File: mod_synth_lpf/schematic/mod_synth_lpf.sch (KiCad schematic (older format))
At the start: 47 parts

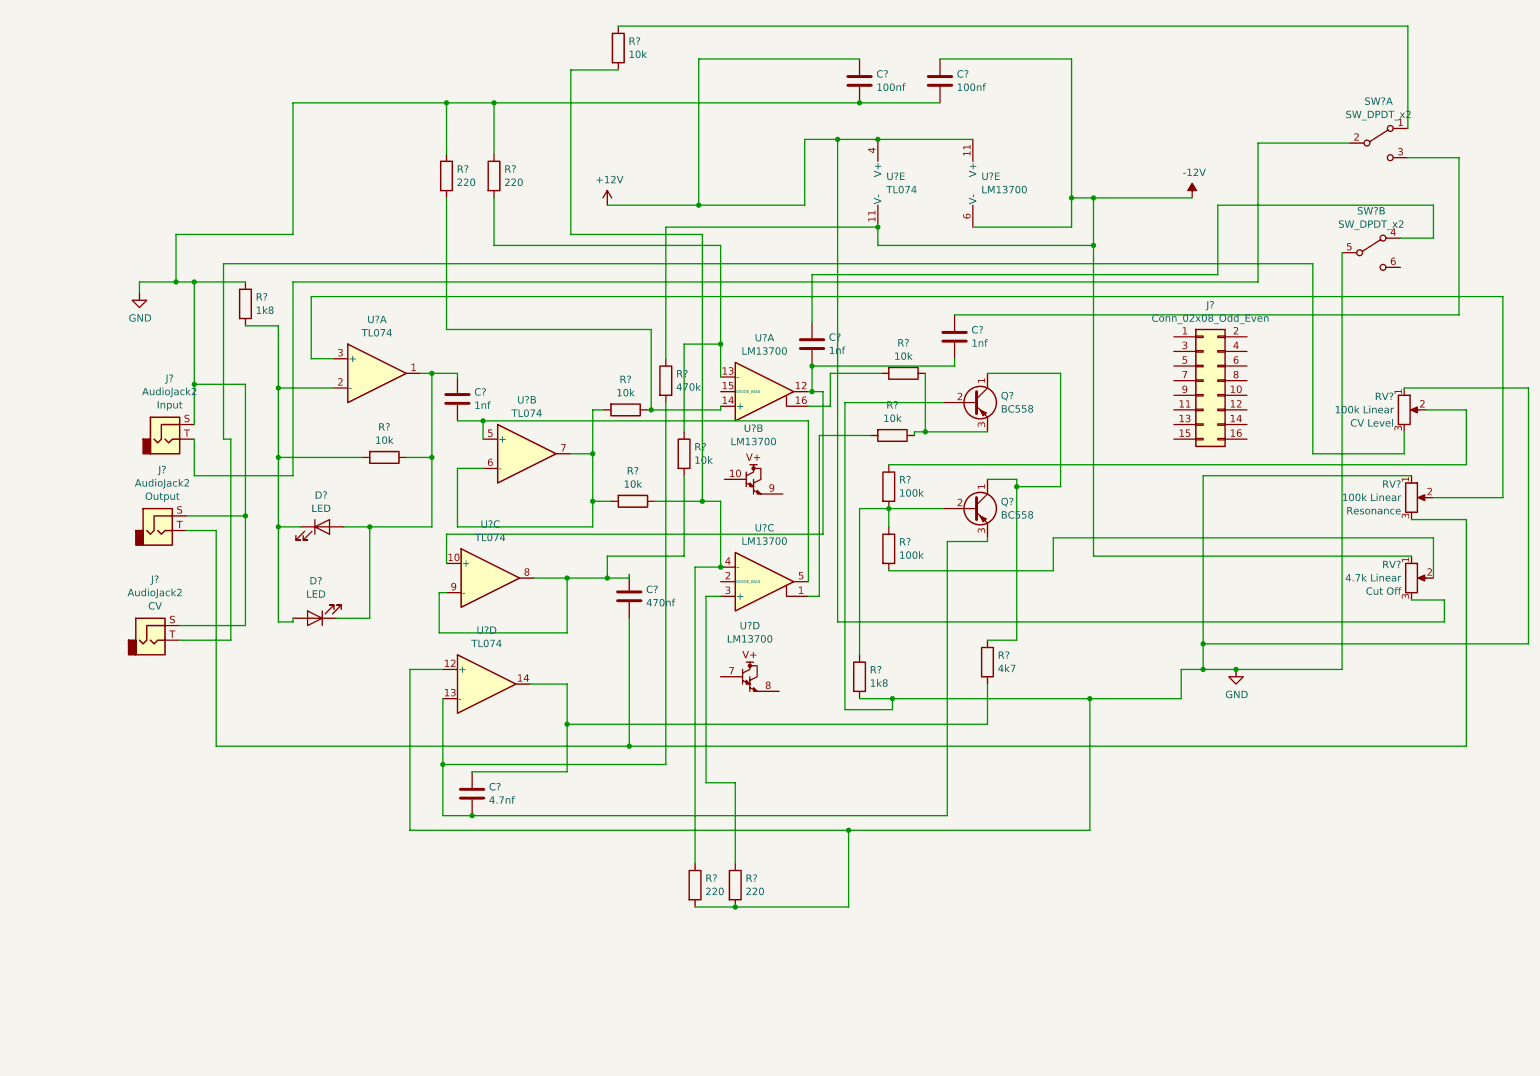
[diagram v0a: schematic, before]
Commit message: Add some footprints to LPF
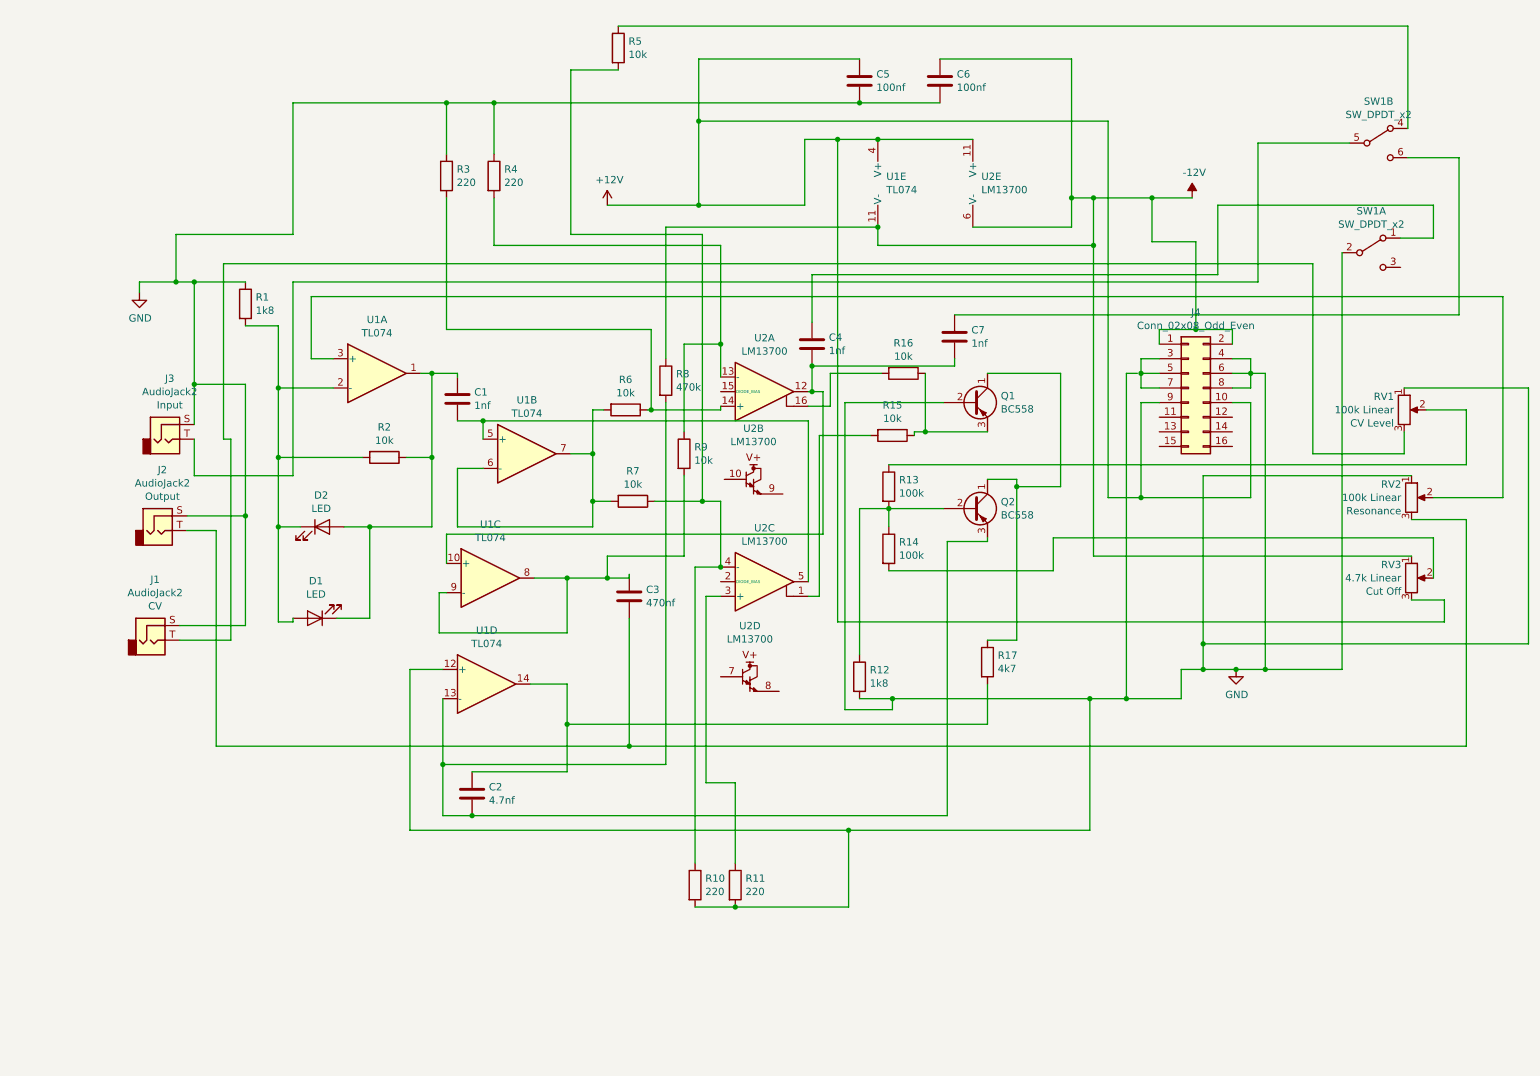
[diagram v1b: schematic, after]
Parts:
- J4: renamed from J?; footprint (none) -> Connector_IDC:IDC-Header_2x08_P2.54mm_Vertical
- RV1, RV2, RV3: renamed from RV?; footprint (none) -> Potentiometer_THT:Potentiometer_Alpha_RD901F-40-00D_Single_Vertical_CircularHoles
- gave numbers to parts that had none: 34
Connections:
- net +12V: now also J4.10 (Pin_10), J4.9 (Pin_9)
- net -12V: now also J4.1 (Pin_1), J4.2 (Pin_2)
- net GND: now also J4.4 (Pin_4), J4.6 (Pin_6), J4.8 (Pin_8), SW1.2 (B); no longer SW1.5 (B)
- net at J4.3 (Pin_3): now also J4.5 (Pin_5), J4.7 (Pin_7)
- net at J3.T: now also SW1.5 (B); no longer SW1.2 (B)
- net at C4.1: now also SW1.1 (A); no longer SW1.4 (A)
- net at C7.1: now also SW1.6 (C); no longer SW1.3 (C)
- net at R5.1: now also SW1.4 (A); no longer SW1.1 (A)
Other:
- moved on the sheet: J4

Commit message: Organise schematic and cram components on PCB
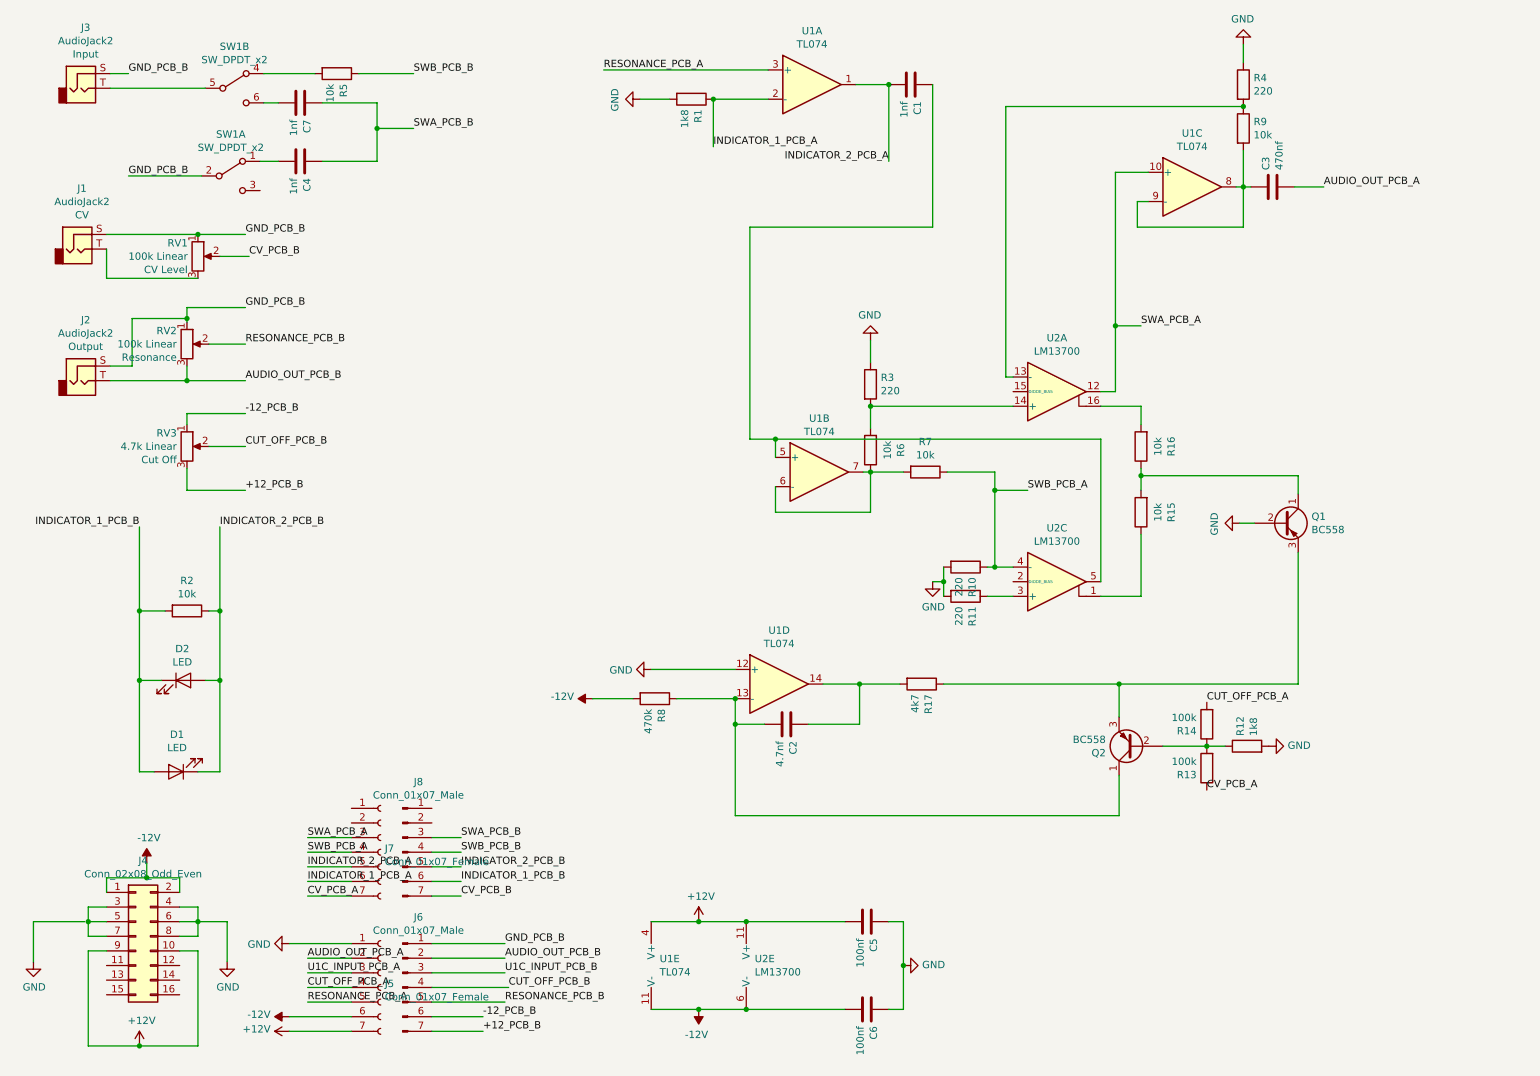
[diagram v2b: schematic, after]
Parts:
- removed unit 2 of U2
- removed unit 4 of U2
- added J5, J7: Conn_01x07_Female, Connector_PinSocket_2.54mm:PinSocket_1x07_P2.54mm_Vertical, symbol Connector:Conn_01x07_Female
- added J6, J8: Conn_01x07_Male, Connector_PinHeader_2.54mm:PinHeader_1x07_P2.54mm_Vertical, symbol Connector:Conn_01x07_Male
- C1, C2, C3, C4, C5, C6, C7: footprint (none) -> Capacitor_THT:C_Disc_D9.0mm_W2.5mm_P5.00mm
- D1, D2: footprint (none) -> LED_THT:LED_D5.0mm
- J1, J2, J3: footprint (none) -> Connector_Audio:Jack_3.5mm_QingPu_WQP-PJ398SM_Vertical_CircularHoles
- R1, R10, R11, R12, R13, R14, R15, R16, R17, R2, R3, R4, R5, R6, R7, R8, R9: footprint (none) -> Resistor_THT:R_Axial_DIN0207_L6.3mm_D2.5mm_P10.16mm_Horizontal
- SW1: footprint (none) -> mod_synth:DPDT_Switch_Vertical
- U1: footprint (none) -> Package_DIP:DIP-14_W7.62mm_Socket_LongPads
- U2: footprint (none) -> Package_DIP:DIP-18_W7.62mm_Socket_LongPads
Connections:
- net +12V: now also C5.2, J5.7 (Pin_7); no longer C5.1, RV3.3
- net -12V: now also C6.2, R8.2, J5.6 (Pin_6); no longer C6.1, R8.1, RV3.1
- net GND: now also C5.1, C6.1, R1.2, J5.1 (Pin_1); no longer C5.2, C6.2, J1.S, J2.S, J3.S, R1.1, RV1.1, RV2.1, SW1.2 (B)
- net INDICATOR_2_PCB_B: now reaches D1.1 (K), D2.2 (A), R2.1
- net INDICATOR_2_PCB_B: now also J8.5 (Pin_5); no longer C1.1, U1.1
- net INDICATOR_1_PCB_B: now reaches D1.2 (A), D2.1 (K), R2.2
- net INDICATOR_1_PCB_B: now also J8.6 (Pin_6); no longer R1.2, U1.2 (-)
- net RESONANCE_PCB_A: now reaches U1.3 (+)
- net RESONANCE_PCB_A: now also J5.5 (Pin_5); no longer RV2.2
- net at U1.5 (+), U2.5: now also C1.1; no longer C1.2
- net at R7.2, U1.6 (-), U1.7: now also R6.1; no longer R6.2
- net SWA_PCB_A: now reaches U1.10 (+), U2.12
- net SWA_PCB_A: now also J7.3 (Pin_3); no longer C4.2, C7.2
- net at C2.2, U1.13 (-): now also Q2.1 (C), R8.1; no longer Q2.3 (E), R8.2
- net at R3.2, U2.14 (+): now also R6.2; no longer R6.1
- net at R15.2: now also Q1.1 (C), R16.1; no longer U2.1
- net SWB_PCB_A: now reaches R10.1, R7.1, U2.4 (-)
- net SWB_PCB_A: now also J7.4 (Pin_4); no longer R5.2
- net CUT_OFF_PCB_A: now reaches R14.2
- net CUT_OFF_PCB_A: now also J5.4 (Pin_4); no longer RV3.2
- net AUDIO_OUT_PCB_B: now reaches J2.T, RV2.3
- net AUDIO_OUT_PCB_B: now also J6.2 (Pin_2); no longer C3.2
- net CV_PCB_A: now reaches R13.1
- net CV_PCB_A: now also J7.7 (Pin_7); no longer RV1.2
- net at SW1.1 (A): now also C4.2; no longer C4.1
- net at SW1.6 (C): now also C7.2; no longer C7.1
- net at SW1.4 (A): now also R5.2; no longer R5.1
- new net: Q1.3 (E), Q2.3 (E), R17.1
- new net: R15.1, U2.1
- new net +12_PCB_B: J6.7 (Pin_7), RV3.3
- new net -12_PCB_B: J6.6 (Pin_6), RV3.1
- new net AUDIO_OUT_PCB_A: C3.2, J5.2 (Pin_2)
- new net CUT_OFF_PCB_B: J6.4 (Pin_4), RV3.2
- new net CV_PCB_B: J8.7 (Pin_7), RV1.2
- new net GND_PCB_B: J1.S, J2.S, J3.S, J6.1 (Pin_1), RV1.1, RV2.1, SW1.2 (B)
- new net INDICATOR_1_PCB_A: J7.6 (Pin_6), R1.1, U1.2 (-)
- new net INDICATOR_2_PCB_A: C1.2, J7.5 (Pin_5), U1.1
- new net RESONANCE_PCB_B: J6.5 (Pin_5), RV2.2
- new net SWA_PCB_B: C4.1, C7.1, J8.3 (Pin_3)
- new net SWB_PCB_B: J8.4 (Pin_4), R5.1
- new net U1C_INPUT_PCB_A: J5.3 (Pin_3)
- new net U1C_INPUT_PCB_B: J6.3 (Pin_3)
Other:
- moved on the sheet: C1, C2, C3, C4, C5, C6, C7, D1, D2, J1, J2, J3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

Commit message: Use 16 pin socket for 16 pin device
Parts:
- U2: footprint Package_DIP:DIP-18_W7.62mm_Socket_LongPads -> Package_DIP:DIP-16_W7.62mm_Socket_LongPads
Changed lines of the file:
@@
 F 0 "U2" H 7650 4867 50  0000 C CNN
 F 1 "LM13700" H 7650 4776 50  0000 C CNN
-F 2 "Package_DIP:DIP-18_W7.62mm_Socket_LongPads" H 7350 4525 50  0001 C CNN
+F 2 "Package_DIP:DIP-16_W7.62mm_Socket_LongPads" H 7350 4525 50  0001 C CNN
 F 3 "http://www.ti.com/lit/ds/symlink/lm13700.pdf" H 7350 4525 50  0001 C CNN
 	3    7650 4500
@@
 F 0 "U2" H 5583 7171 50  0000 L CNN
 F 1 "LM13700" H 5583 7080 50  0000 L CNN
-F 2 "Package_DIP:DIP-18_W7.62mm_Socket_LongPads" H 5325 7150 50  0001 C CNN
+F 2 "Package_DIP:DIP-16_W7.62mm_Socket_LongPads" H 5325 7150 50  0001 C CNN
 F 3 "http://www.ti.com/lit/ds/symlink/lm13700.pdf" H 5325 7150 50  0001 C CNN
 	5    5625 7125
@@
 F 0 "U2" H 7650 3567 50  0000 C CNN
 F 1 "LM13700" H 7650 3476 50  0000 C CNN
-F 2 "Package_DIP:DIP-18_W7.62mm_Socket_LongPads" H 7350 3225 50  0001 C CNN
+F 2 "Package_DIP:DIP-16_W7.62mm_Socket_LongPads" H 7350 3225 50  0001 C CNN
 F 3 "http://www.ti.com/lit/ds/symlink/lm13700.pdf" H 7350 3225 50  0001 C CNN
 	1    7650 3200
